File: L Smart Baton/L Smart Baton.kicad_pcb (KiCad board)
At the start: 2 copper layers, 25 x 200 mm, 51 parts, among them J1 USB4105-GF-A, SW1 B3U-1000P, SW1_R1 1k, U1 MDBT50Q-1MV2, U2 LSM6DSOX, U3 BQ24074RGT, U4 TPS63001

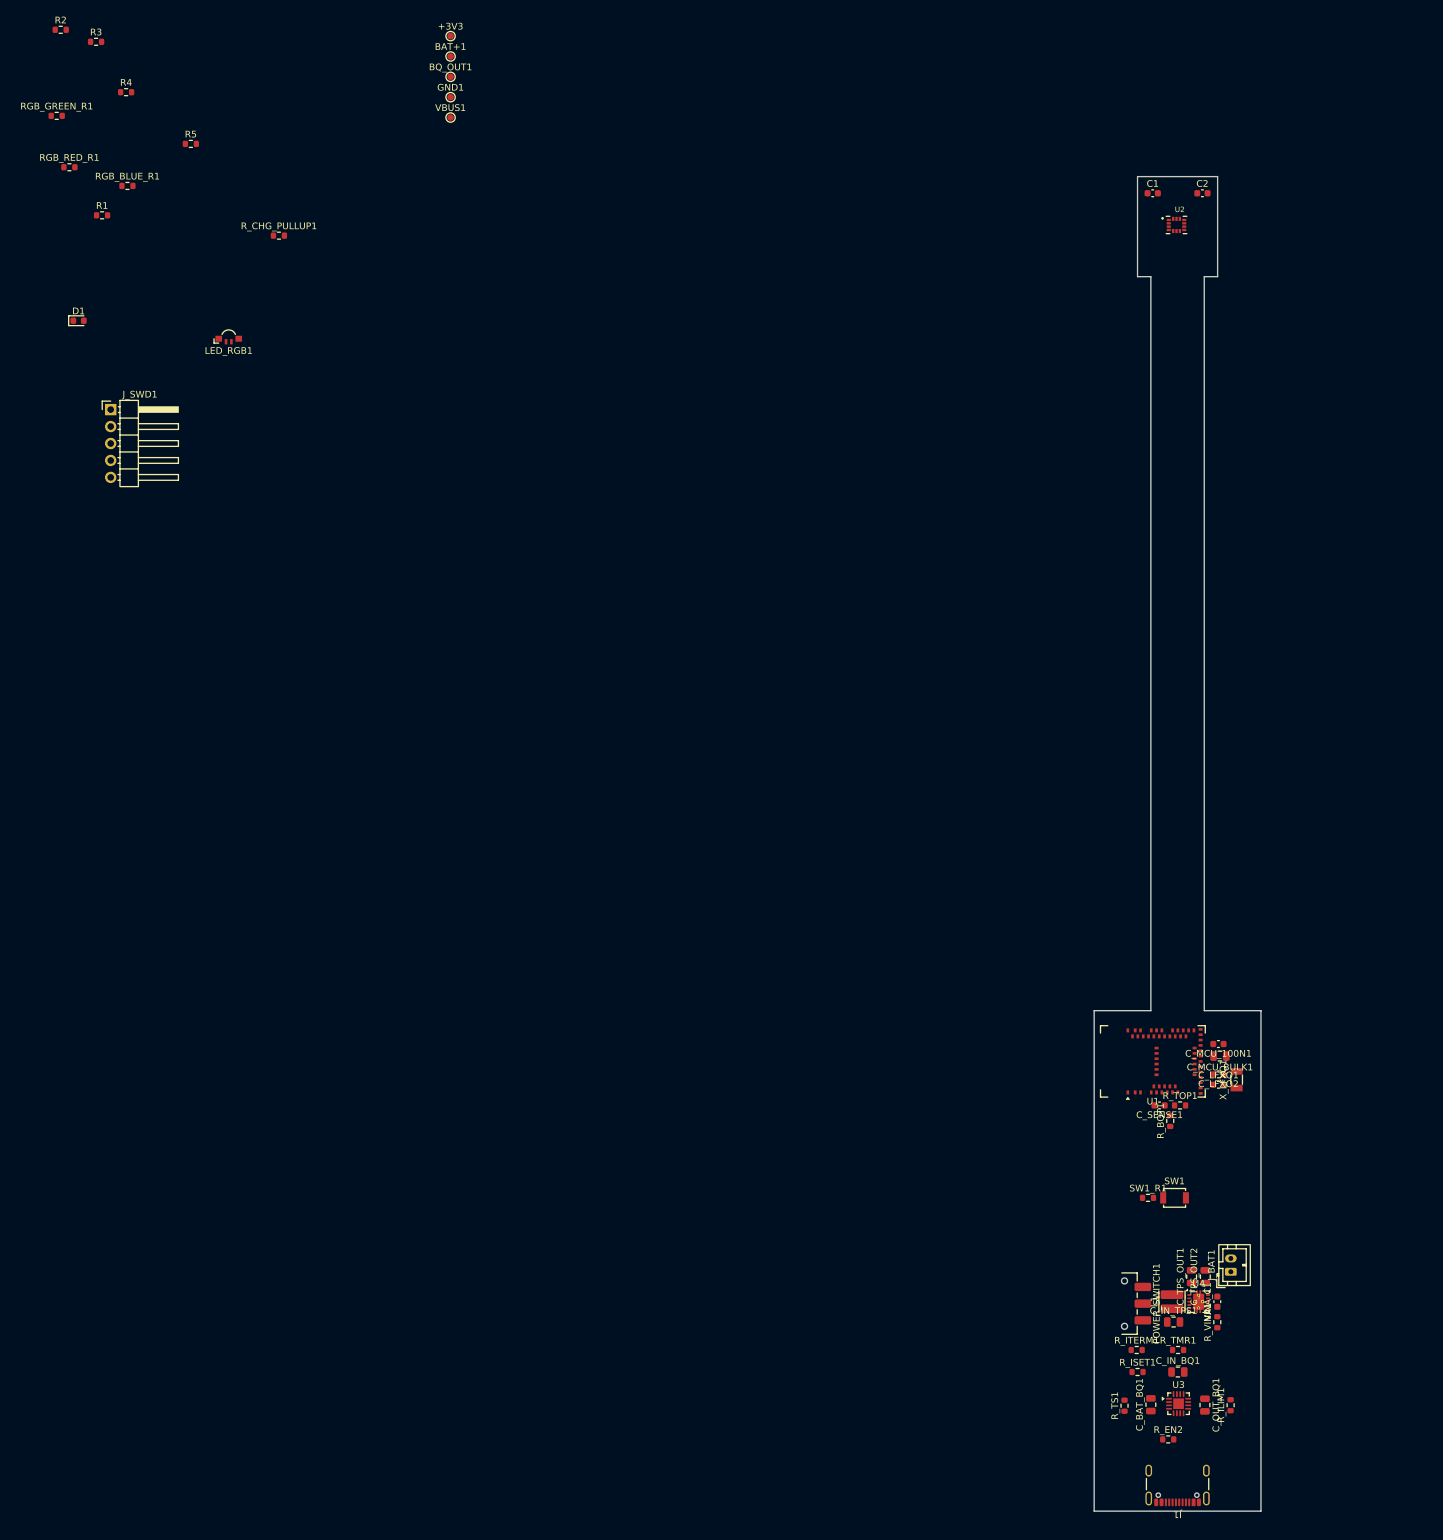
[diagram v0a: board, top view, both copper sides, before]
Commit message: components placed on PCB
Components have been placed on the PCB, only the test pads remain, which I intentionally left for last, to place after routing. It would be easier to know where to place them once the routes have been drawn. Also, the PCB layout has been reviewed by Claude and Chat both of which gave the clear to start routing. Will start routing myself on Sunday afternoon.
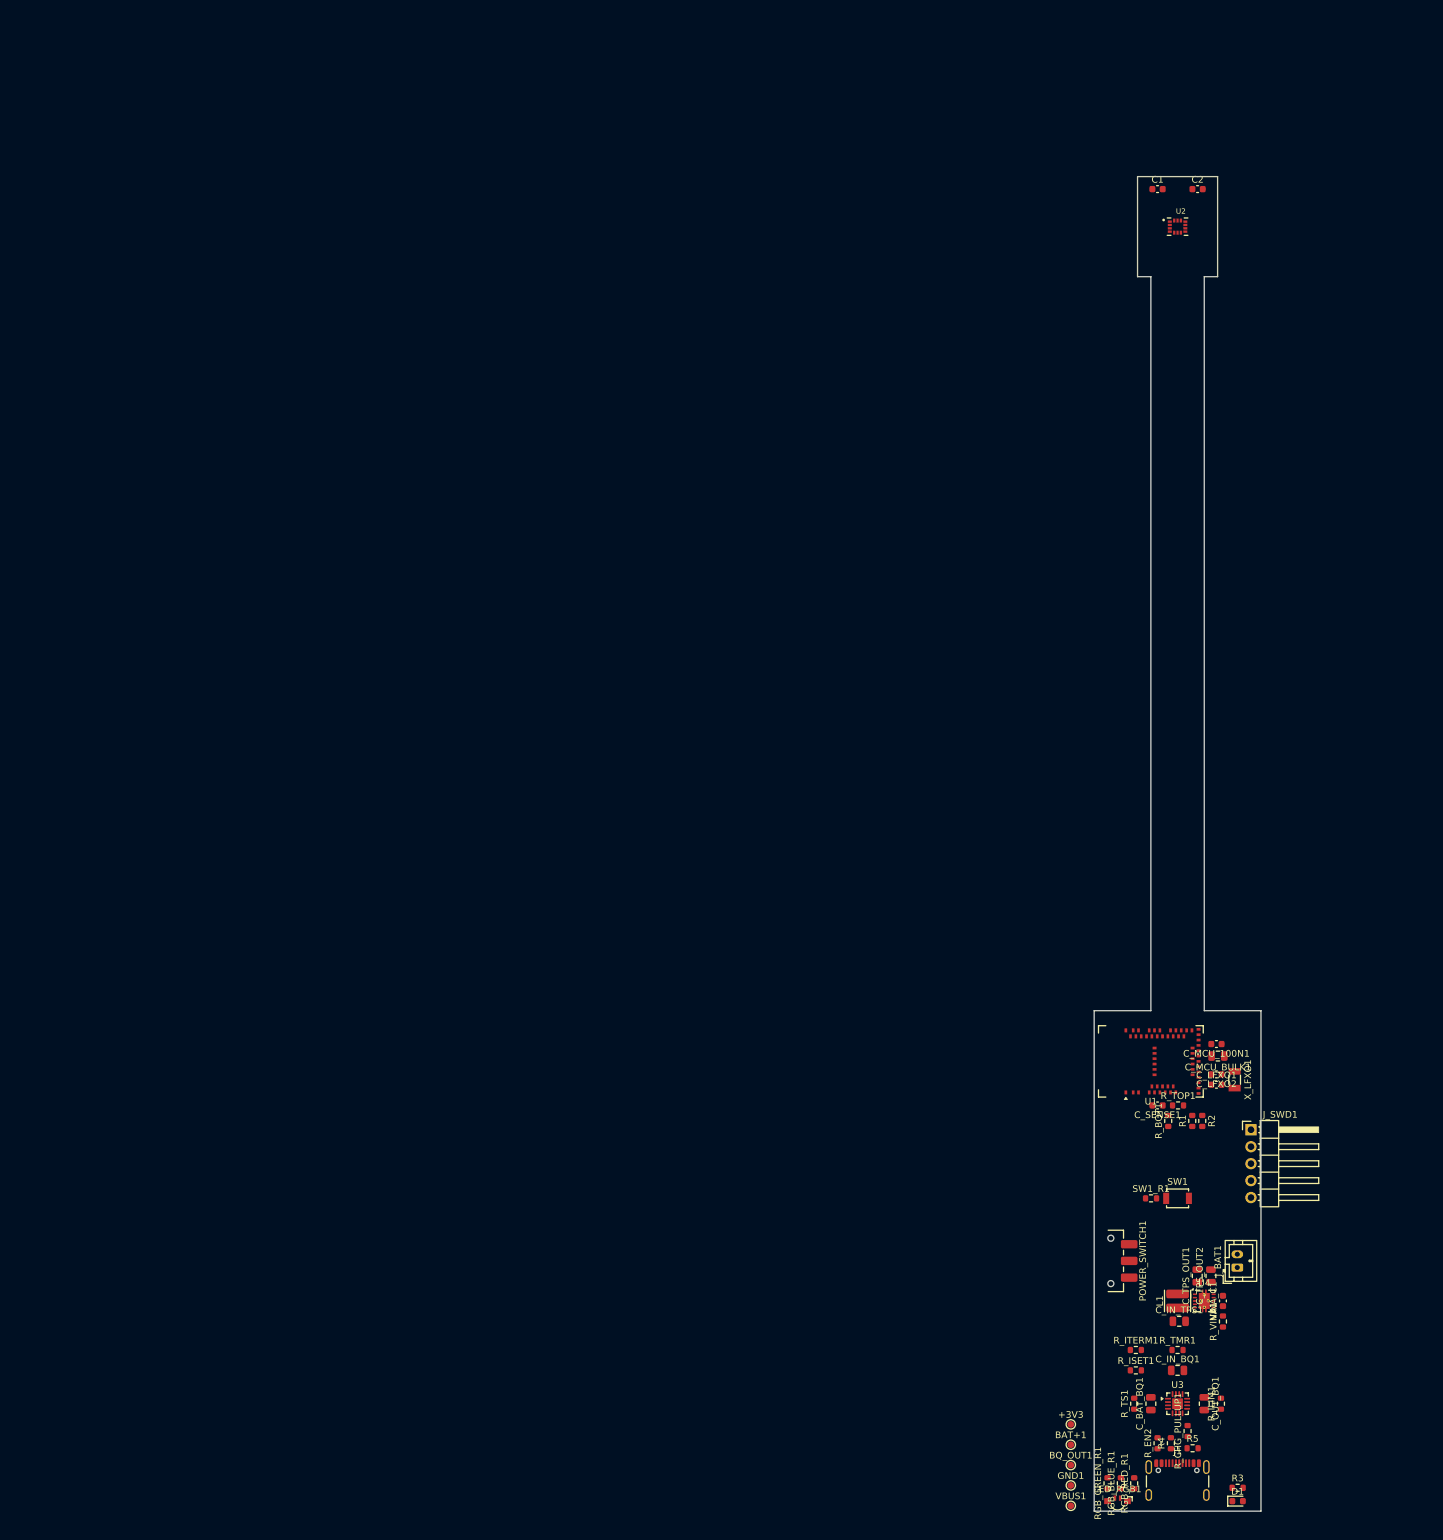
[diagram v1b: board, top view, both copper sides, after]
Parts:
- moved R3 276.1 mm to (201.5, 236.5)
- moved RGB_GREEN_R1 258.4 mm to (182.0, 235.8), turned to 90 degrees
- moved R4 256.0 mm to (191.5, 229.8), turned to 90 degrees
- moved RGB_RED_R1 253.7 mm to (186.0, 235.8), turned to 90 degrees
- moved D1 247.9 mm to (201.5, 238.5)
- moved R5 246.5 mm to (194.8, 230.6)
- moved RGB_BLUE_R1 244.9 mm to (184.0, 235.8), turned to 90 degrees
- moved R2 236.7 mm to (196.2, 181.5), turned to -90 degrees
- moved +3V3 227.9 mm to (176.5, 227.0)
- moved BAT+1 227.9 mm to (176.5, 230.1)
- moved GND1 227.9 mm to (176.5, 236.2)
- moved BQ_OUT1 227.9 mm to (176.5, 233.1)
- moved VBUS1 227.9 mm to (176.5, 239.2)
- moved R_CHG_PULLUP1 225.0 mm to (194.0, 228.0), turned to 90 degrees
- moved LED_RGB1 219.3 mm to (183.5, 238.5), turned to 180 degrees
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
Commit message: layout iteration + measurements
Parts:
- added REF**: MountingHole_2.1mm, MountingHole:MountingHole_2.1mm, F.Cu at (192.5, 199.0)
- added REF**: MountingHole_2.1mm, MountingHole:MountingHole_2.1mm, F.Cu at (201.1, 228.9)
- added REF**: MountingHole_2.1mm, MountingHole:MountingHole_2.1mm, F.Cu at (183.9, 228.9)
- moved C1 70.4 mm to (191.0, 112.2), turned to -90 degrees
- moved C2 70.4 mm to (194.0, 112.2), turned to 90 degrees
- moved U2 69.0 mm to (192.5, 116.5)
- moved BQ_OUT1 31.1 mm to (202.5, 216.0)
- moved BAT+1 30.8 mm to (202.5, 213.5)
- moved VBUS1 30.4 mm to (202.5, 223.5)
- moved GND1 30.1 mm to (202.5, 221.0)
- moved +3V3 27.4 mm to (202.5, 218.5)
- moved C_LFXO1 5.49 mm to (199.3, 181.5)
- moved C_MCU_100N1 5.49 mm to (199.3, 175.4)
- moved C_SENSE1 5.49 mm to (190.5, 184.6)
- moved R1 5.49 mm to (195.7, 186.9)
- moved R2 5.49 mm to (197.2, 186.9)
- moved R_BOT1 5.49 mm to (192.1, 186.9)
- moved R_TOP1 5.49 mm to (193.6, 184.6)
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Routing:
- net GND: track 0.00 -> 17.8 mm, vias 0 -> 8
- net +3V3: track 0.00 -> 11.0 mm
- net Net-(POWER_SWITCH1-A): track 0.00 -> 10.7 mm
- net Net-(U4-VINA): track 0.00 -> 3.20 mm
- net Net-(U4-L2): track 0.00 -> 2.83 mm
- net Net-(U4-L1): track 0.00 -> 2.83 mm
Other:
- board size 25 x 200 mm -> 23 x 130 mm

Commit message: Pre auto-routing save
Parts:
- moved +3V3 58.2 mm to (220.0, 163.0)
- moved BAT+1 58.2 mm to (220.0, 158.0)
- moved BQ_OUT1 58.2 mm to (220.0, 160.5)
- moved GND1 58.2 mm to (220.0, 165.5)
- moved VBUS1 58.2 mm to (220.0, 168.0)
- moved J_SWD1 53.8 mm to (220.0, 135.4)
- moved J_BAT1 53.6 mm to (217.9, 152.5)
- moved C_BAT_BQ1 53.4 mm to (206.0, 173.4)
- moved C_IN_BQ1 53.4 mm to (210.0, 168.4)
- moved C_MCU_100N1 53.4 mm to (216.8, 124.9)
- moved C_OUT_BQ1 53.4 mm to (214.0, 173.4)
- moved C_SENSE1 53.4 mm to (208.0, 134.1)
- moved D1 53.4 mm to (218.5, 188.0)
- moved J1 53.4 mm to (210.0, 186.0)
- moved LED_RGB1 53.4 mm to (201.0, 188.0)
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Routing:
- net Net-(U1-P0.26): track 0.00 -> 94.6 mm
- net Net-(U1-P0.27): track 0.00 -> 92.2 mm, vias 0 -> 2
- net /IMU_INT2: track 0.00 -> 60.3 mm, vias 0 -> 2
- net /IMU_INT1: track 0.00 -> 57.2 mm
- net +3V3: track 11.0 -> 30.0 mm, vias 0 -> 5
- net GND: track 17.8 -> 26.7 mm, vias 8 -> 12
- net Net-(U1-P0.01): track 0.00 -> 6.04 mm
- net Net-(U1-P0.00): track 0.00 -> 6.00 mm

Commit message: Post shaft length change draft (LATEST)
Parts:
- moved U2 47.0 mm to (210.0, 113.0)
- moved C1 46.8 mm to (208.8, 108.8)
- moved C2 46.8 mm to (211.2, 108.8)
- moved R_BOT1 0.10 mm to (209.5, 136.4)
- turned R_ITERM1 to 180 degrees
- turned R_TS1 to -90 degrees
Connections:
- U1 pad 22: unconnected-(U1-P0.06-Pad22) -> /BLE_LED
- U1 pad 43: /BLE_LED -> unconnected-(U1-P0.21-Pad43)
- U1 pad 46: /RGB_RED -> unconnected-(U1-P0.22-Pad46)
- U1 pad 47: unconnected-(U1-P1.00-Pad47) -> /RGB_RED
- U1 pad 48: /RGB_BLUE -> unconnected-(U1-P0.24-Pad48)
- U1 pad 49: unconnected-(U1-P0.25-Pad49) -> /RGB_BLUE
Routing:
- net +3V3: track 30.0 -> 174.9 mm, vias 5 -> 13
- net /RGB_GREEN: track 0.00 -> 69.6 mm, vias 0 -> 2
- net /BLE_LED: track 0.00 -> 68.1 mm, vias 0 -> 4
- net /RGB_BLUE: track 0.00 -> 66.8 mm, vias 0 -> 2
- net /RGB_RED: track 0.00 -> 66.5 mm, vias 0 -> 2
- net GND: track 26.7 -> 89.6 mm, vias 12 -> 20
- net Net-(U1-P0.27): track 92.2 -> 30.2 mm
- net Net-(J_BAT1-Pin_1): track 0.00 -> 62.0 mm, vias 0 -> 2
- net /CHG_STATUS: track 0.00 -> 62.0 mm, vias 0 -> 4
- net /SW_POW: track 0.00 -> 52.8 mm, vias 0 -> 4
- net Net-(U1-P0.26): track 94.6 -> 45.1 mm
- net /IMU_INT2: track 60.3 -> 11.5 mm
- net /IMU_INT1: track 57.2 -> 10.2 mm
- net Net-(U3-IN): track 0.00 -> 35.3 mm, vias 0 -> 6
- net Net-(POWER_SWITCH1-A): track 10.7 -> 40.5 mm
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- added copper zone on B.Cu, net GND
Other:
- board size 23 x 130 mm -> 23 x 83 mm

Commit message: Final PCB layout
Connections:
- U1 pad 43: unconnected-(U1-P0.21-Pad43) -> (no net)
- U1 pad 46: unconnected-(U1-P0.22-Pad46) -> (no net)
- U1 pad 48: unconnected-(U1-P0.24-Pad48) -> (no net)
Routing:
- net GND: track 89.6 -> 91.6 mm
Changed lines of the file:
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@@
 		(filling no)
 		(pcbplotparams
-			(layerselection 0x00000000_00000000_55555555_5755f5ff)
-			(plot_on_all_layers_selection 0x00000000_00000000_00000000_00000000)
+			(layerselection 0x00000000_00000000_5555575f_5f55df50)
+			(plot_on_all_layers_selection 0x00000000_00000000_0000020a_0a008a00)
 			(disableapertmacros no)
-			(usegerberextensions no)
-			(usegerberattributes yes)
+			(usegerberextensions yes)
+			(usegerberattributes no)
 			(usegerberadvancedattributes yes)
 			(creategerberjobfile yes)
@@
 			(dashed_line_gap_ratio 3)
 			(svgprecision 4)
-			(plotframeref no)
+			(plotframeref yes)
 			(mode 1)
-			(useauxorigin no)
+			(useauxorigin yes)
 			(pdf_front_fp_property_popups yes)
 			(pdf_back_fp_property_popups yes)
-			(pdf_metadata yes)
+			(pdf_metadata no)
 			(pdf_single_document no)
 			(dxfpolygonmode yes)
@@
 			(psnegative no)
 			(psa4output no)
-			(plot_black_and_white yes)
+			(plot_black_and_white no)
 			(sketchpadsonfab no)
 			(plotpadnumbers no)
-			(hidednponfab no)
-			(sketchdnponfab yes)
-			(crossoutdnponfab yes)
+			(hidednponfab yes)
+			(sketchdnponfab no)
+			(crossoutdnponfab no)
 			(subtractmaskfromsilk no)
-			(outputformat 1)
+			(outputformat 4)
 			(mirror no)
-			(drillshape 1)
+			(drillshape 0)
 			(scaleselection 1)
-			(outputdirectory "")
+			(outputdirectory "C:/Users/jalkh.m/Downloads/")
 		)
 	)
@@
 				(pins "51" "53" "11" "9" "20" "21" "13" "10" "14" "12" "52" "54" "34"
 					"35" "61" "50" "60" "56" "59" "57" "58" "25" "3" "4" "5" "6" "7" "8"
-					"28" "30" "1" "33" "2" "15" "55" "32" "31" "17" "18" "22" "24" "37"
+					"28" "30" "1" "33" "55" "2" "15" "32" "31" "17" "18" "22" "24" "37"
 					"36" "39" "38" "41" "40" "42" "44" "43" "46" "45" "48" "49" "19" "16"
 					"47" "29" "27" "26" "23"
@@
 			(size 0.6 0.4)
 			(layers "F.Cu" "F.Mask" "F.Paste")
-			(net "unconnected-(U1-P0.21-Pad43)")
 			(pinfunction "P0.21_43")
-			(pintype "bidirectional")
+			(pintype "no_connect")
 		)
 		(pad "44" smd rect
@@
 			(size 0.6 0.4)
 			(layers "F.Cu" "F.Mask" "F.Paste")
-			(net "unconnected-(U1-P0.22-Pad46)")
 			(pinfunction "P0.22_46")
-			(pintype "bidirectional")
+			(pintype "no_connect")
 		)
 		(pad "47" smd rect
@@
 			(size 0.6 0.4)
 			(layers "F.Cu" "F.Mask" "F.Paste")
-			(net "unconnected-(U1-P0.24-Pad48)")
 			(pinfunction "P0.24_48")
-			(pintype "bidirectional")
+			(pintype "no_connect")
 		)
 		(pad "49" smd rect
@@
 			(type default)
 		)
+		(locked yes)
 		(layer "Edge.Cuts")
 	)
@@
 			(type default)
 		)
+		(locked yes)
 		(layer "Edge.Cuts")
 	)
@@
 			(type default)
 		)
+		(locked yes)
 		(layer "Edge.Cuts")
 	)
@@
 			(type default)
 		)
+		(locked yes)
 		(layer "Edge.Cuts")
 	)
@@
 			(type default)
 		)
+		(locked yes)
 		(layer "Edge.Cuts")
 	)
@@
 			(type default)
 		)
+		(locked yes)
 		(layer "Edge.Cuts")
 	)
@@
 			(type default)
 		)
+		(locked yes)
 		(layer "Edge.Cuts")
 	)
@@
 			(type default)
 		)
+		(locked yes)
 		(layer "Edge.Cuts")
 	)
@@
 	)
 	(segment
+		(start 204.35 133.75)
+		(end 204.35 132.15)
+		(width 0.3)
+		(layer "F.Cu")
+		(net "GND")
+	)
+	(segment
 		(start 209.75 173.65)
 		(end 210 173.4)
@@
 	)
 	(segment
+		(start 203.25 121.65)
+		(end 203.25 122.85)
+		(width 0.3)
+		(layer "F.Cu")
+		(net "GND")
+	)
+	(segment
 		(start 217.6 129.5)
 		(end 217.556293 129.5)
@@
 	)
 	(segment
+		(start 204 120.5)
+		(end 204 120.9)
+		(width 0.3)
+		(layer "F.Cu")
+		(net "GND")
+	)
+	(segment
 		(start 213.075 182.195)
 		(end 213.2 182.32)
@@
 	)
 	(segment
+		(start 203.732147 134.367854)
+		(end 204.35 133.75)
+		(width 0.3)
+		(layer "F.Cu")
+		(net "GND")
+	)
+	(segment
 		(start 213.55 123.5)
 		(end 214.15 123.5)
@@
 	)
 	(segment
-		(start 203.25 121.65)
-		(end 203.25 122.85)
-		(width 0.3)
-		(layer "F.Cu")
-		(net "GND")
-	)
-	(segment
 		(start 206.05 161.05)
 		(end 207.3 161.05)
@@
 	)
 	(segment
+		(start 204 120.9)
+		(end 203.25 121.65)
+		(width 0.3)
+		(layer "F.Cu")
+		(net "GND")
+	)
+	(segment
 		(start 212.575 157.646447)
 		(end 212.575 158)
@@
 	)
 	(segment
-		(start 203.5 121.4)
-		(end 203.25 121.65)
-		(width 0.3)
-		(layer "F.Cu")
-		(net "GND")
-	)
-	(segment
-		(start 204.35 133.75)
-		(end 204.35 132.15)
-		(width 0.3)
-		(layer "F.Cu")
-		(net "GND")
-	)
-	(segment
 		(start 218.4 124.9)
 		(end 219.5 126)
@@
 	)
 	(via
-		(at 203.5 121.4)
+		(at 204 120.5)
 		(size 0.6)
 		(drill 0.3)
@@
 	)
 	(via
-		(at 204.35 133.75)
+		(at 203.732147 134.367854)
 		(size 0.6)
 		(drill 0.3)
@@
 	)
 	(segment
-		(start 208.75 123.571698)
-		(end 208.75 123.75)
-		(width 0.25)
-		(layer "F.Cu")
-		(net "unconnected-(U1-P0.21-Pad43)")
-	)
-	(segment
 		(start 208.45 125.050001)
 		(end 208.762654 124.737347)
@@
 	(zone
 		(net "GND")
+		(locked yes)
 		(layer "B.Cu")
 		(hatch edge 0.5)
@@
 		(polygon
 			(pts
-				(xy 199 107) (xy 221 107) (xy 221 189) (xy 199 189)
+				(xy 221 189) (xy 199 189) (xy 199 134) (xy 204.5 134) (xy 204.5 121) (xy 199 121) (xy 199 107) (xy 221 107)
 			)
 		)
